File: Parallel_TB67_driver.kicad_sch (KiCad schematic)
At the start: 6 parts, among them J1 Vin, J2 Vout, J3 Driver_pinout, J4 MotorA, J5 MotorB, U1 Driver Module

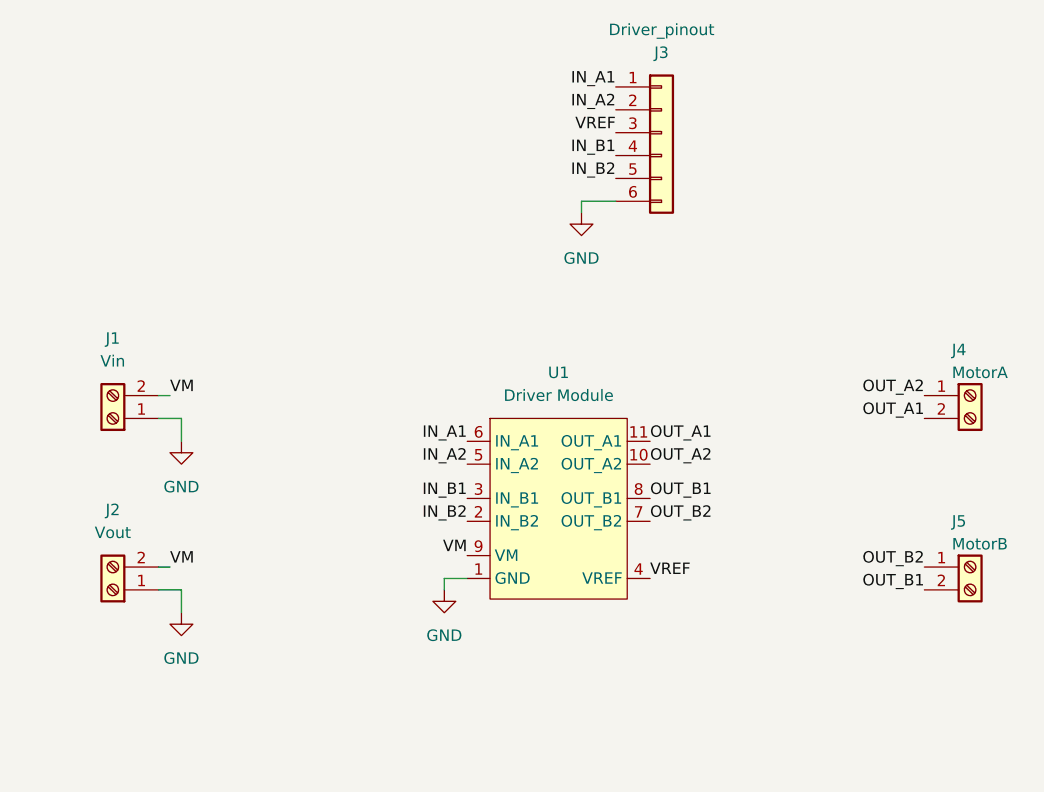
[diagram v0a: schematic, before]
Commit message: Capacitors sch & components placement
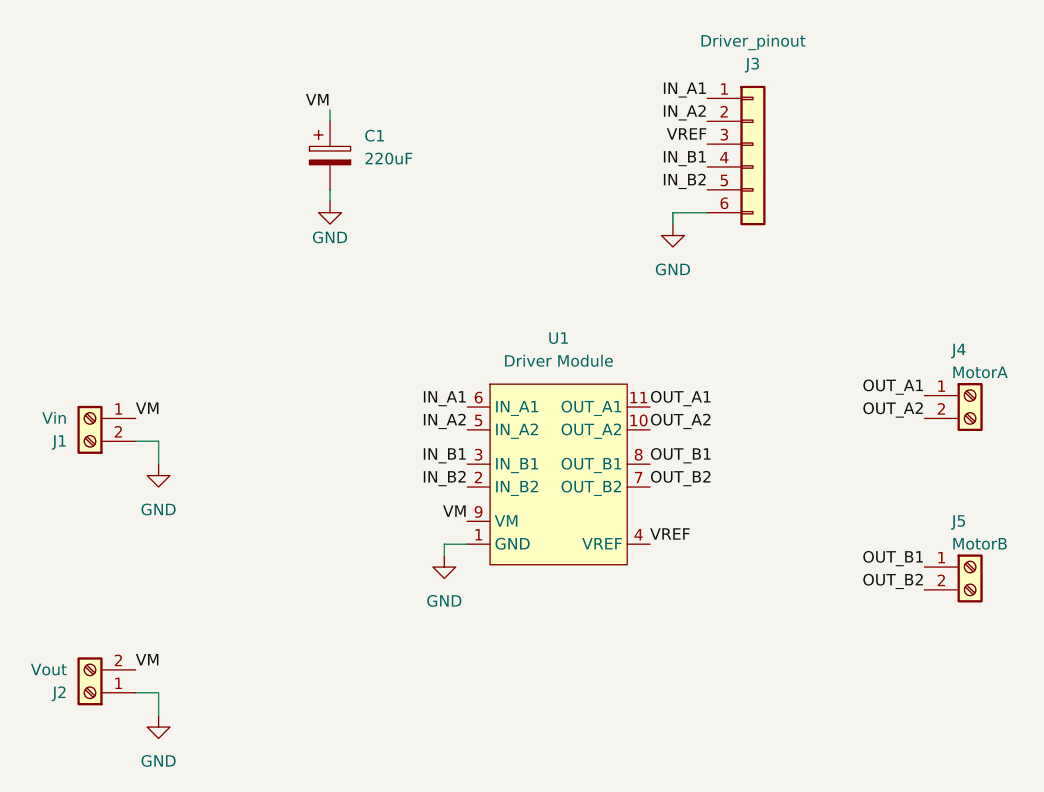
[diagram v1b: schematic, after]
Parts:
- added C1: 220uF, Capacitor_THT:CP_Radial_D10.0mm_P3.50mm, symbol Device:C_Polarized
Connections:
- net GND: now also J1.2 (Pin_1), C1.2; no longer J1.1 (Pin_1)
- net OUT_A1: now also J4.1 (Pin_1); no longer J4.2 (Pin_2)
- net OUT_A2: now also J4.2 (Pin_2); no longer J4.1 (Pin_1)
- net OUT_B1: now also J5.1 (Pin_1); no longer J5.2 (Pin_2)
- net OUT_B2: now also J5.2 (Pin_2); no longer J5.1 (Pin_1)
- net VM: now also J1.1 (Pin_2), C1.1; no longer J1.2 (Pin_2)
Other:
- moved on the sheet: J1, J2, J3, U1
